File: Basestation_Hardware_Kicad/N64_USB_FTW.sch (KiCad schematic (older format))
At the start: 28 parts, among them IC1 ATMEGA8-AI, U1 LM317, X1 12mhz, X2 USB

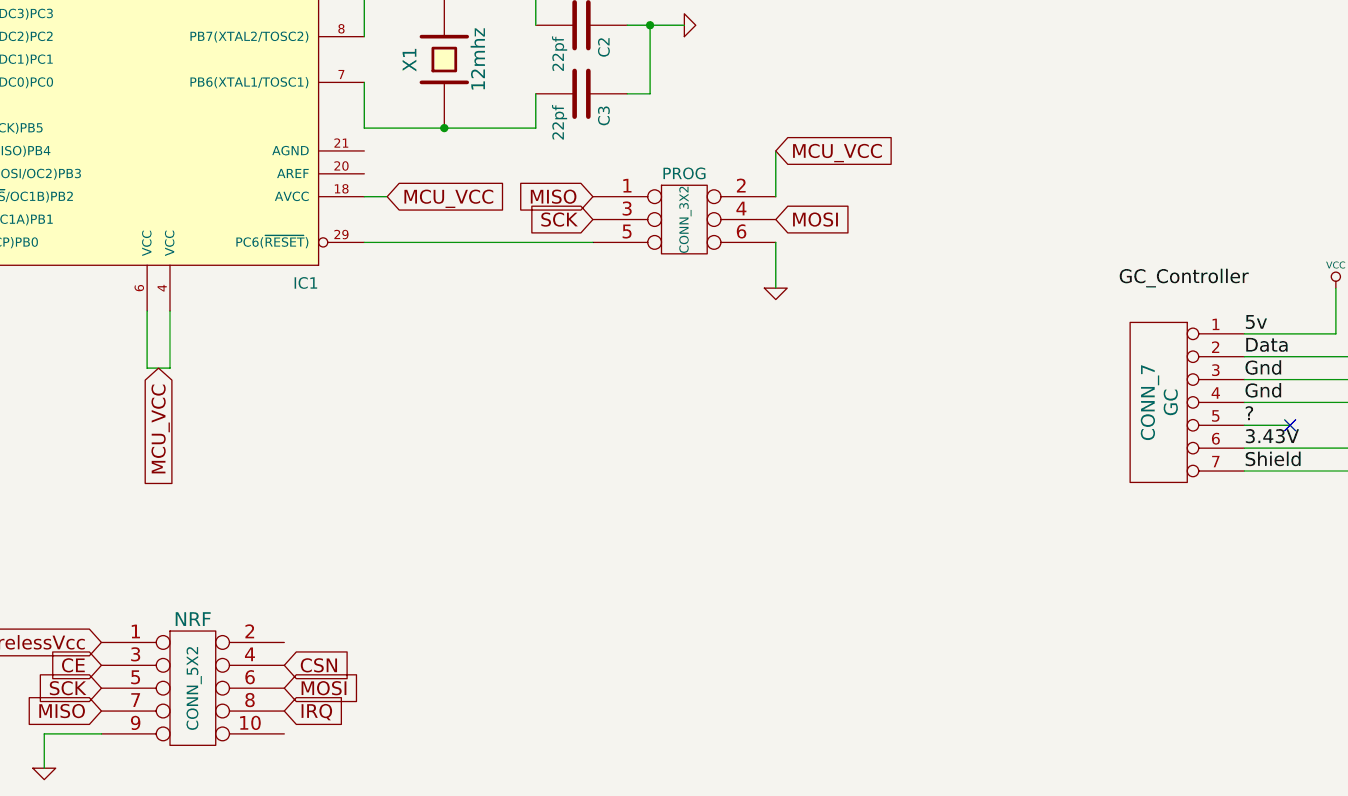
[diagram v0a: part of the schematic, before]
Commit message: load caps on xtals changed from 27pf to 22pf
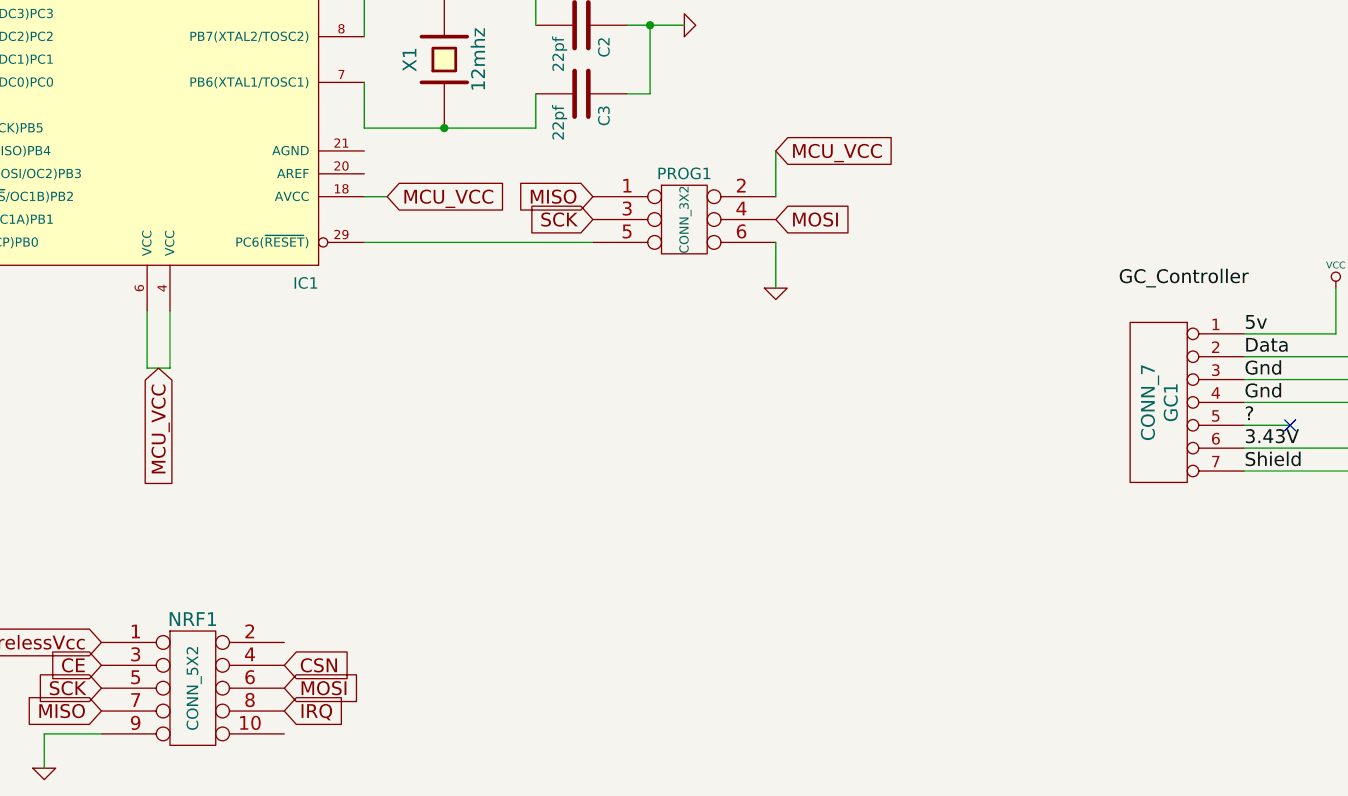
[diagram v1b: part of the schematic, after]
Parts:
- renumbered GC to GC1, NRF to NRF1, PROG to PROG1
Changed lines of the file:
@@
-EESchema Schematic File Version 2  date 19-06-2012 12:50:49
+EESchema Schematic File Version 2  date 19-06-2012 13:26:47
 LIBS:power
 LIBS:device
@@
 MCU_VCC
 $Comp
-L CONN_5X2 NRF
+L CONN_5X2 NRF1
 U 1 1 4F68E2A7
 P 6950 6750
-F 0 "NRF" H 6950 7050 60  0000 C CNN
+F 0 "NRF1" H 6950 7050 60  0000 C CNN
 F 1 "CONN_5X2" V 6950 6750 50  0000 C CNN
 	1    6950 6750
@@
 $EndComp
 $Comp
-L GND #PWR01
+L GND #PWR17
 U 1 1 4F56953B
 P 12000 2950
-F 0 "#PWR01" H 12000 2950 30  0001 C CNN
+F 0 "#PWR17" H 12000 2950 30  0001 C CNN
 F 1 "GND" H 12000 2880 30  0001 C CNN
 	1    12000 2950
@@
 $EndComp
 $Comp
-L GND #PWR02
+L GND #PWR15
 U 1 1 4F56949A
 P 10600 3050
-F 0 "#PWR02" H 10600 3050 30  0001 C CNN
+F 0 "#PWR15" H 10600 3050 30  0001 C CNN
 F 1 "GND" H 10600 2980 30  0001 C CNN
 	1    10600 3050
@@
 $EndComp
 $Comp
-L GND #PWR03
+L GND #PWR7
 U 1 1 4F5646E2
 P 4450 4700
-F 0 "#PWR03" H 4450 4700 30  0001 C CNN
+F 0 "#PWR7" H 4450 4700 30  0001 C CNN
 F 1 "GND" H 4450 4630 30  0001 C CNN
 	1    4450 4700
@@
 $EndComp
 $Comp
-L GND #PWR04
+L GND #PWR4
 U 1 1 4F563B84
 P 3600 5700
-F 0 "#PWR04" H 3600 5700 30  0001 C CNN
+F 0 "#PWR4" H 3600 5700 30  0001 C CNN
 F 1 "GND" H 3600 5630 30  0001 C CNN
 	1    3600 5700
@@
 $EndComp
 $Comp
-L VCC #PWR05
+L VCC #PWR12
 U 1 1 4F563AF3
 P 9350 2200
-F 0 "#PWR05" H 9350 2300 30  0001 C CNN
+F 0 "#PWR12" H 9350 2300 30  0001 C CNN
 F 1 "VCC" H 9350 2300 30  0000 C CNN
 	1    9350 2200
@@
 MCU_VCC
 $Comp
-L GND #PWR06
+L GND #PWR1
 U 1 1 4F4E474C
 P 1800 4050
-F 0 "#PWR06" H 1800 4050 30  0001 C CNN
+F 0 "#PWR1" H 1800 4050 30  0001 C CNN
 F 1 "GND" H 1800 3980 30  0001 C CNN
 	1    1800 4050
@@
 $EndComp
 $Comp
-L GND #PWR07
+L GND #PWR3
 U 1 1 4F4D32A1
 P 3150 5700
-F 0 "#PWR07" H 3150 5700 30  0001 C CNN
+F 0 "#PWR3" H 3150 5700 30  0001 C CNN
 F 1 "GND" H 3150 5630 30  0001 C CNN
 	1    3150 5700
@@
 SCK
 $Comp
-L GND #PWR08
+L GND #PWR8
 U 1 1 4F4D25F3
 P 6300 7100
-F 0 "#PWR08" H 6300 7100 30  0001 C CNN
+F 0 "#PWR8" H 6300 7100 30  0001 C CNN
 F 1 "GND" H 6300 7030 30  0001 C CNN
 	1    6300 7100
@@
 $EndComp
 $Comp
-L GND #PWR09
+L GND #PWR19
 U 1 1 4F4D1C43
 P 12300 4050
-F 0 "#PWR09" H 12300 4050 30  0001 C CNN
+F 0 "#PWR19" H 12300 4050 30  0001 C CNN
 F 1 "GND" H 12300 3980 30  0001 C CNN
 	1    12300 4050
@@
 $EndComp
 $Comp
-L GND #PWR010
+L GND #PWR18
 U 1 1 4F452EB3
 P 12200 6250
-F 0 "#PWR010" H 12200 6250 30  0001 C CNN
+F 0 "#PWR18" H 12200 6250 30  0001 C CNN
 F 1 "GND" H 12200 6180 30  0001 C CNN
 	1    12200 6250
@@
 Controller Data
 $Comp
-L VCC #PWR011
+L VCC #PWR16
 U 1 1 4F452CF5
 P 11950 5000
-F 0 "#PWR011" H 11950 5100 30  0001 C CNN
+F 0 "#PWR16" H 11950 5100 30  0001 C CNN
 F 1 "VCC" H 11950 5100 30  0000 C CNN
 	1    11950 5000
@@
 GC_Controller
 $Comp
-L CONN_7 GC
+L CONN_7 GC1
 U 1 1 4F452C08
 P 11200 5500
-F 0 "GC" V 11170 5500 60  0000 C CNN
+F 0 "GC1" V 11170 5500 60  0000 C CNN
 F 1 "CONN_7" V 11270 5500 60  0000 C CNN
 	1    11200 5500
@@
 $EndComp
 $Comp
-L GND #PWR012
+L GND #PWR20
 U 1 1 4F45295F
 P 12850 3050
-F 0 "#PWR012" H 12850 3050 30  0001 C CNN
+F 0 "#PWR20" H 12850 3050 30  0001 C CNN
 F 1 "GND" H 12850 2980 30  0001 C CNN
 	1    12850 3050
@@
 $EndComp
 $Comp
-L GND #PWR013
+L GND #PWR14
 U 1 1 4F45213D
 P 9900 2950
-F 0 "#PWR013" H 9900 2950 30  0001 C CNN
+F 0 "#PWR14" H 9900 2950 30  0001 C CNN
 F 1 "GND" H 9900 2880 30  0001 C CNN
 	1    9900 2950
@@
 $EndComp
 $Comp
-L GND #PWR014
+L GND #PWR11
 U 1 1 4F440011
 P 9100 3850
-F 0 "#PWR014" H 9100 3850 30  0001 C CNN
+F 0 "#PWR11" H 9100 3850 30  0001 C CNN
 F 1 "GND" H 9100 3780 30  0001 C CNN
 	1    9100 3850
@@
 pc5
 $Comp
-L GND #PWR015
+L GND #PWR9
 U 1 1 4F43FD84
 P 6750 2200
-F 0 "#PWR015" H 6750 2200 30  0001 C CNN
+F 0 "#PWR9" H 6750 2200 30  0001 C CNN
 F 1 "GND" H 6750 2130 30  0001 C CNN
 	1    6750 2200
@@
 $EndComp
 $Comp
-L GND #PWR016
+L GND #PWR10
 U 1 1 4F43FD6B
 P 6850 2200
-F 0 "#PWR016" H 6850 2200 30  0001 C CNN
+F 0 "#PWR10" H 6850 2200 30  0001 C CNN
 F 1 "GND" H 6850 2130 30  0001 C CNN
 	1    6850 2200
@@
 $EndComp
 $Comp
-L GND #PWR017
+L GND #PWR13
 U 1 1 4F43FC5C
 P 9500 5000
-F 0 "#PWR017" H 9500 5000 30  0001 C CNN
+F 0 "#PWR13" H 9500 5000 30  0001 C CNN
 F 1 "GND" H 9500 4930 30  0001 C CNN
 	1    9500 5000
@@
 SCK
 $Comp
-L GND #PWR018
+L GND #PWR2
 U 1 1 4F43F2E9
 P 3100 4750
-F 0 "#PWR018" H 3100 4750 30  0001 C CNN
+F 0 "#PWR2" H 3100 4750 30  0001 C CNN
 F 1 "GND" H 3100 4680 30  0001 C CNN
 	1    3100 4750
@@
 $EndComp
 $Comp
-L GND #PWR019
+L GND #PWR6
 U 1 1 4F43EE47
 P 3800 4750
-F 0 "#PWR019" H 3800 4750 30  0001 C CNN
+F 0 "#PWR6" H 3800 4750 30  0001 C CNN
 F 1 "GND" H 3800 4680 30  0001 C CNN
 	1    3800 4750
@@
 $EndComp
 $Comp
-L CONN_3X2 PROG
+L CONN_3X2 PROG1
 U 1 1 4F43E0D8
 P 9100 4750
-F 0 "PROG" H 9100 5000 50  0000 C CNN
+F 0 "PROG1" H 9100 5000 50  0000 C CNN
 F 1 "CONN_3X2" V 9100 4800 40  0000 C CNN
 	1    9100 4750
@@
 $EndComp
 $Comp
-L VCC #PWR020
+L VCC #PWR5
 U 1 1 4F43DEFD
 P 3650 2900
-F 0 "#PWR020" H 3650 3000 30  0001 C CNN
+F 0 "#PWR5" H 3650 3000 30  0001 C CNN
 F 1 "VCC" H 3650 3000 30  0000 C CNN
 	1    3650 2900

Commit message: oh my god, bargraph
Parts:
- added BAR1: DOT-BAR2, symbol DOT-BAR2
- added R10, R6, R9: 40, symbol R
- R5: value 10k -> 40
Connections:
- net ControllerVcc: no longer IC1.23 ((ADC0)PC0), R5.2
- net GND: no longer R5.1
- net Charlie 1: now reaches IC1.24 ((ADC1)PC1)
- net Charlie 1: now also R6.2
- net Charlie 2: now reaches IC1.25 ((ADC2)PC2)
- net Charlie 2: now also R9.2
- net Charlie 3: now reaches IC1.26 ((ADC3)PC3)
- net Charlie 3: now also R10.2
- new net: BAR1.1 (A), BAR1.12 (K), BAR1.15 (K), BAR1.2 (A), BAR1.3 (A), R5.1
- new net: BAR1.10 (A), BAR1.14 (K), BAR1.17 (K), BAR1.20 (K), R10.1
- new net: BAR1.11 (K), BAR1.16 (K), BAR1.19 (K), BAR1.7 (A), BAR1.8 (A), BAR1.9 (A), R9.1
- new net: BAR1.13 (K), BAR1.18 (K), BAR1.4 (A), BAR1.5 (A), BAR1.6 (A), R6.1
- new net Charlie 0: IC1.23 ((ADC0)PC0), R5.2
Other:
- note added: "3210"
- note added: "LHZZ"
- note added: "LZHZ"
- note added: "LZZH"
- note added: "ZHLZ"
- note added: "ZHZL"
- note added: "ZLHZ"
- note added: "ZLZH"
- note added: "ZZHL"
- note added: "ZZLH"

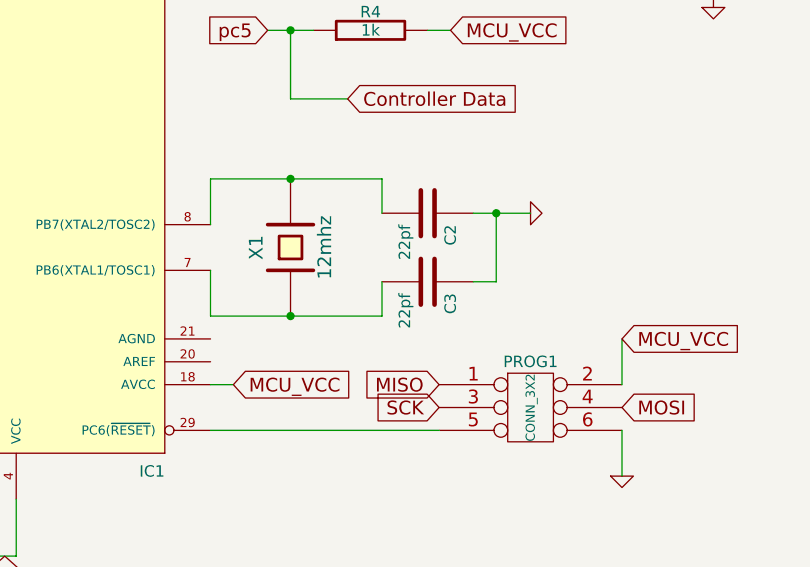
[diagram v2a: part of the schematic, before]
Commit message: changed xtal footprint, added fancy schmancy silk-logo
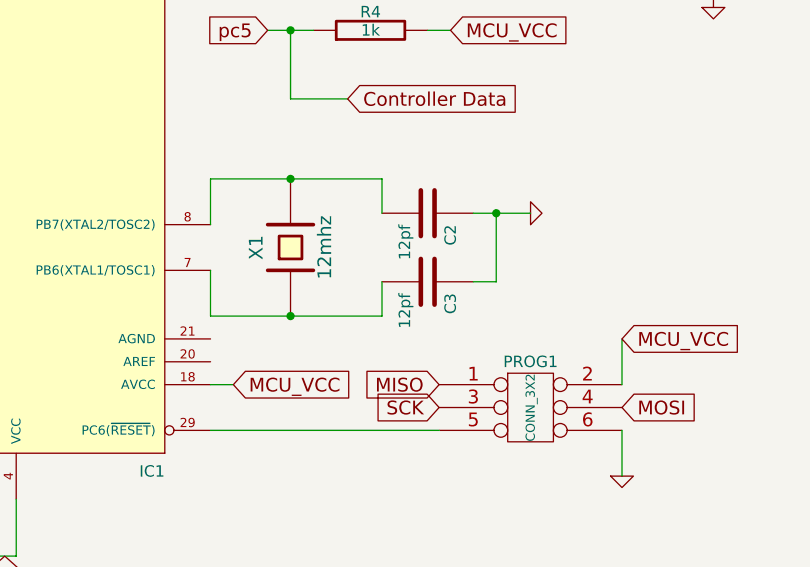
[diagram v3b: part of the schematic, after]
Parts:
- C2, C3: value 22pf -> 12pf
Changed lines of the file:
@@
-EESchema Schematic File Version 2  date 26-06-2012 15:50:33
+EESchema Schematic File Version 2  date 21-08-2012 09:10:22
 LIBS:power
 LIBS:device
@@
 Sheet 1 1
 Title ""
-Date "26 jun 2012"
+Date "21 aug 2012"
 Rev ""
 Comp ""
@@
 P 8650 3850
 F 0 "C2" H 8700 3950 50  0000 L CNN
-F 1 "22pf" H 8700 3750 50  0000 L CNN
+F 1 "12pf" H 8700 3750 50  0000 L CNN
 	1    8650 3850
 	0    1    1    0
@@
 P 8650 4150
 F 0 "C3" H 8700 4250 50  0000 L CNN
-F 1 "22pf" H 8700 4050 50  0000 L CNN
+F 1 "12pf" H 8700 4050 50  0000 L CNN
 	1    8650 4150
 	0    1    1    0

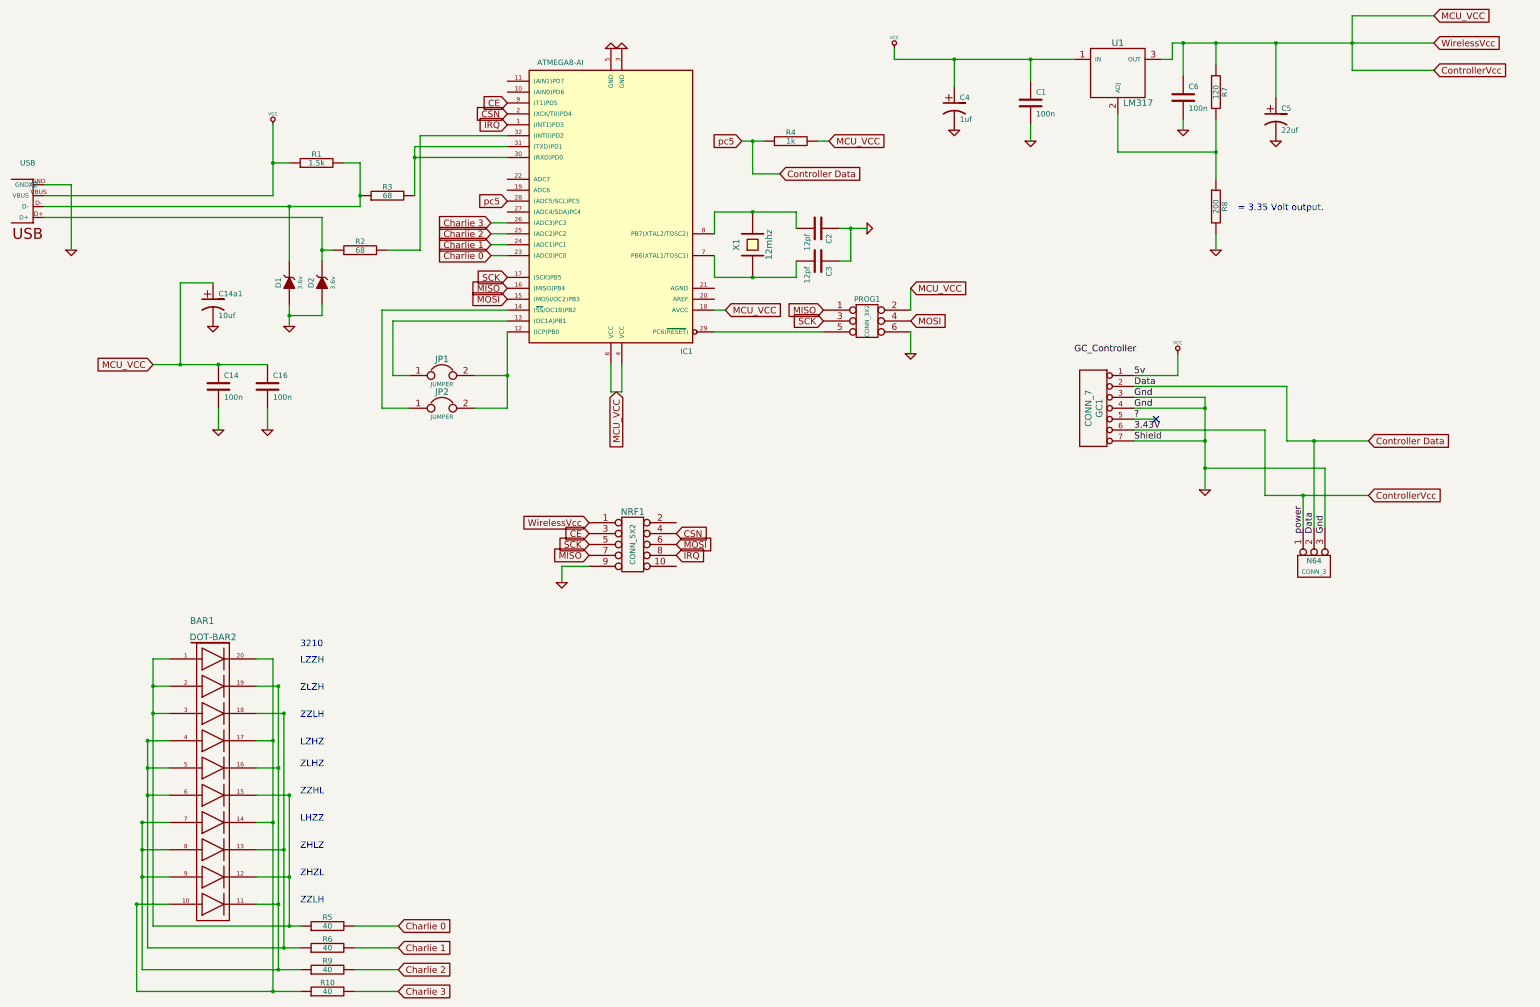
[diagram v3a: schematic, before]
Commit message: mistakes taken care of: moved, drill holes, changed regulator to lm1117, nudged gnd-plane to make more room for NRF module antenna
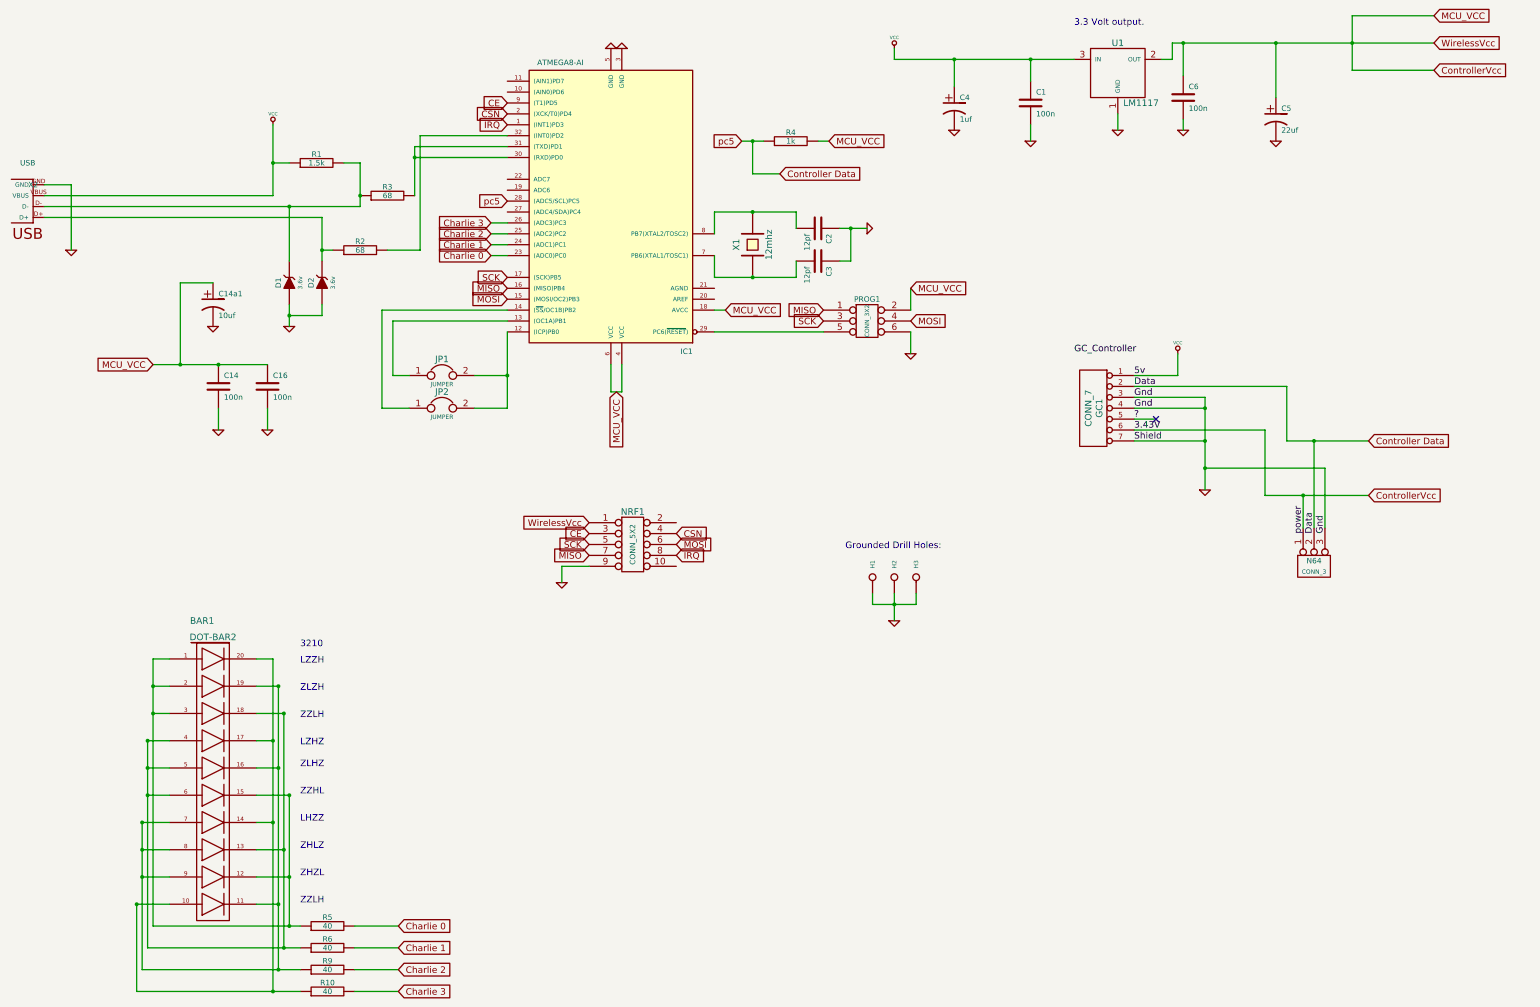
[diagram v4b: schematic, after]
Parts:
- removed R7: 120, symbol R
- removed R8: 200, symbol R
- removed U1: LM317, symbol LM317
- added H1, H2, H3: CONN_1, symbol CONN_1
- added U1: LM1117, symbol LM1117
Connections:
- net ControllerVcc: now also U1.2 (OUT)
- net GND: now also H1.1, H2.1, H3.1, U1.1 (GND)
- net VCC: now also U1.3 (IN)
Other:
- note added: "3.3 Volt output."
- note added: "Grounded Drill Holes:"
- note removed: "= 3.35 Volt output."
